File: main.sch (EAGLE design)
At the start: 116 parts, among them IC10 FGPMMOPA6H, IC2 25LC1024-I/P, IC6 MPL3115A2LGA, IC7 FXAS21000, IC8 ADXL343BCCZ, Q1 12MHz, Q2 MCP9700A-E/TO, Q3 FQP7P06, Q4 MCP9700A-E/TO, U1 ATMEGA1284P-PU, U2 LT3570EFEPBF, U3 TL431BQLP, X1 132134RP

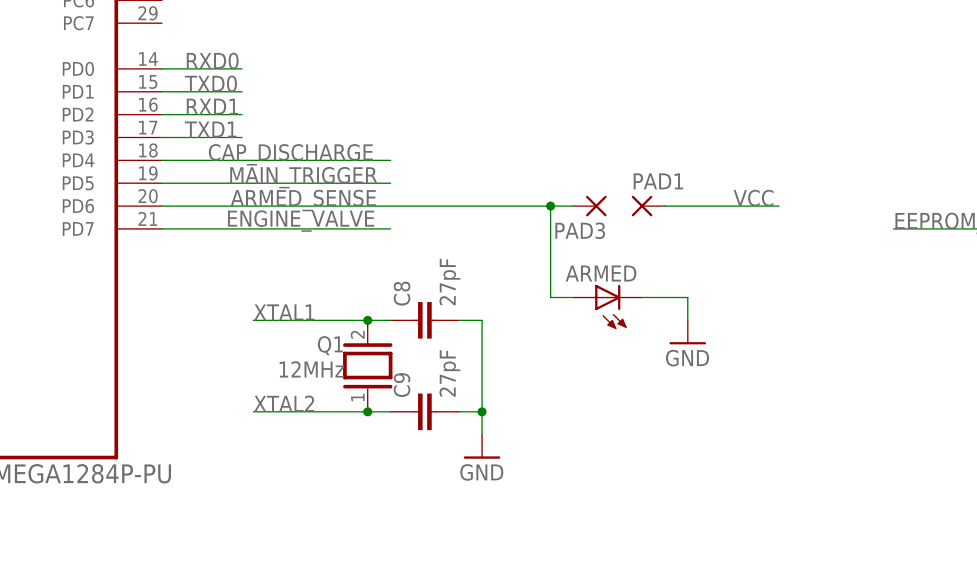
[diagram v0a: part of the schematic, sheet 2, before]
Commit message: Changed armed sense so that the pin is pulled low when armed and added resistor for armed LED.
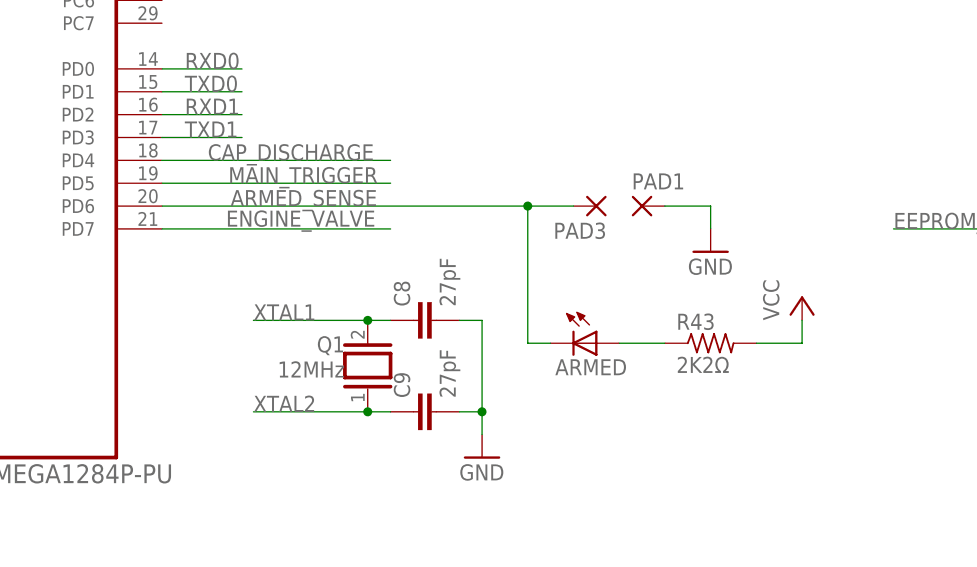
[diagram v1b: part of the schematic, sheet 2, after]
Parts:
- added R43: 2K2Ω, rcl:R-US_0207/5V
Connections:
- new net N$33: ARMED.A, R43.1
- net ARMED_SENSE: now also ARMED.C; no longer ARMED.A
- net GND: now also PAD1.P; no longer ARMED.C
- net VCC: now also R43.2; no longer PAD1.P
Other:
- moved on the sheet: ARMED
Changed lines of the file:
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@@
 <?xml version="1.0" encoding="utf-8"?>
 <!DOCTYPE eagle SYSTEM "eagle.dtd">
-<eagle version="8.6.0">
+<eagle version="8.5.1">
 <drawing>
 <settings>
@@
 <part name="ARMED" library="led" library_urn="urn:adsk.eagle:library:259" deviceset="LED" device="5MM" package3d_urn="urn:adsk.eagle:package:15799/2"/>
 <part name="GND35" library="supply1" library_urn="urn:adsk.eagle:library:371" deviceset="GND" device=""/>
+<part name="R43" library="rcl" library_urn="urn:adsk.eagle:library:334" deviceset="R-US_" device="0207/5V" package3d_urn="urn:adsk.eagle:package:23502/1" value="2K2Ω"/>
+<part name="P+8" library="supply1" library_urn="urn:adsk.eagle:library:371" deviceset="VCC" device=""/>
 </parts>
 <sheets>
@@
 <instance part="PAD1" gate="1" x="134.62" y="114.3"/>
 <instance part="PAD3" gate="1" x="129.54" y="114.3" rot="R180"/>
-<instance part="ARMED" gate="G$1" x="129.54" y="104.14" rot="R90"/>
-<instance part="GND35" gate="1" x="139.7" y="99.06"/>
+<instance part="ARMED" gate="G$1" x="129.54" y="99.06" rot="R270"/>
+<instance part="GND35" gate="1" x="142.24" y="109.22"/>
+<instance part="R43" gate="G$1" x="142.24" y="99.06"/>
+<instance part="P+8" gate="VCC" x="152.4" y="104.14"/>
 </instances>
 <busses>
@@
 </segment>
 <segment>
-<pinref part="ARMED" gate="G$1" pin="C"/>
-<wire x1="134.62" y1="104.14" x2="139.7" y2="104.14" width="0.1524" layer="91"/>
-<wire x1="139.7" y1="104.14" x2="139.7" y2="101.6" width="0.1524" layer="91"/>
+<pinref part="PAD1" gate="1" pin="P"/>
 <pinref part="GND35" gate="1" pin="GND"/>
+<wire x1="137.16" y1="114.3" x2="142.24" y2="114.3" width="0.1524" layer="91"/>
+<wire x1="142.24" y1="114.3" x2="142.24" y2="111.76" width="0.1524" layer="91"/>
 </segment>
 </net>
@@
 </segment>
 <segment>
-<wire x1="137.16" y1="114.3" x2="149.86" y2="114.3" width="0.1524" layer="91"/>
-<label x="144.78" y="114.3" size="1.778" layer="95"/>
-<pinref part="PAD1" gate="1" pin="P"/>
+<pinref part="P+8" gate="VCC" pin="VCC"/>
+<wire x1="152.4" y1="101.6" x2="152.4" y2="99.06" width="0.1524" layer="91"/>
+<pinref part="R43" gate="G$1" pin="2"/>
+<wire x1="152.4" y1="99.06" x2="147.32" y2="99.06" width="0.1524" layer="91"/>
 </segment>
 </net>
@@
 <label x="88.9" y="114.3" size="1.778" layer="95"/>
 <pinref part="U1" gate="A" pin="PD6"/>
-<wire x1="81.28" y1="114.3" x2="124.46" y2="114.3" width="0.1524" layer="91"/>
+<wire x1="81.28" y1="114.3" x2="121.92" y2="114.3" width="0.1524" layer="91"/>
 <pinref part="PAD3" gate="1" pin="P"/>
-<pinref part="ARMED" gate="G$1" pin="A"/>
-<wire x1="124.46" y1="114.3" x2="127" y2="114.3" width="0.1524" layer="91"/>
-<wire x1="124.46" y1="114.3" x2="124.46" y2="104.14" width="0.1524" layer="91"/>
-<wire x1="124.46" y1="104.14" x2="127" y2="104.14" width="0.1524" layer="91"/>
-<junction x="124.46" y="114.3"/>
+<pinref part="ARMED" gate="G$1" pin="C"/>
+<wire x1="121.92" y1="114.3" x2="127" y2="114.3" width="0.1524" layer="91"/>
+<wire x1="124.46" y1="99.06" x2="121.92" y2="99.06" width="0.1524" layer="91"/>
+<wire x1="121.92" y1="99.06" x2="121.92" y2="114.3" width="0.1524" layer="91"/>
+<junction x="121.92" y="114.3"/>
 </segment>
 </net>
@@
 </segment>
 </net>
+<net name="N$33" class="0">
+<segment>
+<pinref part="R43" gate="G$1" pin="1"/>
+<pinref part="ARMED" gate="G$1" pin="A"/>
+<wire x1="137.16" y1="99.06" x2="132.08" y2="99.06" width="0.1524" layer="91"/>
+</segment>
+</net>

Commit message: Fixed ERC errors and renumbered all components.
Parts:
- removed C33, C34: 0.1µF, rcl:C-EU025-025X050
- removed IC8: ADXL343BCCZ, CU in Space:ADXL343BCCZ
- removed U$10, U$9: TEST, Power:TEST
- added C25: 22µF, Power:UST1V220MDD
- added C29: 10nF, Power:K103K15X7RF5TL2
- added IC5: 25LC1024-I/P, microchip:25LC080P
- added U$7: CAP, Power:TEST
- added U$8: BAT+, Power:TEST
- ARMED: value (none) -> RED
- C10: value 47pF -> 0.1µF
- C11: value 1µF -> 0.1µF
- C12: value 1nF -> 0.1µF; device Power:K102K15X7RF5TL2 -> rcl:C-EU025-025X050
- C13, C14: value 22µF -> 0.1µF; device Power:UST1V220MDD -> rcl:C-EU025-025X050
- C15: value 1nF -> 2.2µF; device Power:K102K15X7RF5TL2 -> rcl:C-EU025-025X050
- C16: value 10nF -> 27pF; device Power:K103K15X7RF5TL2 -> rcl:C-EU025-025X050
- C17: value 0.1µF -> 27pF
- C19: value 22µF -> 47pF; device Power:UST1V220MDD -> rcl:C-EU025-025X050
- C20: value 0.1µF -> 1µF
- C26, C27: value 0.1µF -> 22µF; device rcl:C-EU025-025X050 -> Power:UST1V220MDD
- C30: value 10µF -> 1nF; device rcl:CPOL-USE2-5 -> Power:K102K15X7RF5TL2
- C31: value 10µF -> 10nF; device rcl:CPOL-USE2-5 -> Power:K103K15X7RF5TL2
- C32: value 0.1µF -> 1nF; device rcl:C-EU025-025X050 -> Power:K102K15X7RF5TL2
- C4: value 2.2µF -> 0.1µF
- C6: value 0.1µF -> 10µF; device rcl:C-EU025-025X050 -> rcl:CPOL-USE2-5
- C7: value 10nF -> 0.1µF; device Power:K103K15X7RF5TL2 -> rcl:C-EU025-025X050
- C8: value 27pF -> 10µF; device rcl:C-EU025-025X050 -> rcl:CPOL-USE2-5
- C9: value 27pF -> 0.1µF
- IC2: value 25LC1024-I/P -> ADXL343BCCZ; device microchip:25LC080P -> CU in Space:ADXL343BCCZ
- L1: value 18µH -> 10µH; device Power:RLB0914-180KL -> rcl:L-US0207/5V
- L2: value 10µH -> 18µH; device rcl:L-US0207/5V -> Power:RLB0914-180KL
- Q1: value 12MHz -> MCP9700A-E/TO; device special:XTAL/S -> CU in Space:MCP9700A-E/TO
- Q3: value FQP7P06 -> 12MHz; device Power:FQP7P06 -> special:XTAL/S
- Q4: value MCP9700A-E/TO -> FQP7P06; device CU in Space:MCP9700A-E/TO -> Power:FQP7P06
- R10: value 24.9kΩ -> 2K2Ω; device Power:MFR-25FBF52-24K9 -> rcl:R-US_0207/5V
- R11: value 24.9kΩ -> 1MΩ; device Power:MFR-25FBF52-24K9 -> rcl:R-US_0207/5V
- R12: value 51.1kΩ -> 1M; device Power:MFR-25FBF52-51K1 -> Power:MFR-25FBF52-3K65
- R13: value 17.4kΩ -> 3.6k; device Power:MFR-25FBF52-17K4 -> Power:MFR-25FBF52-3K65
- R14: value 3.65kΩ -> 1MΩ; device Power:MFR-25FBF52-3K65 -> rcl:R-US_0207/5V
- R15, R16: value 51.1kΩ -> 750; device Power:MFR-25FBF52-51K1 -> Power:MFR-25FBF52-3K65
- R17, R18: value 47kΩ -> 750; device rcl:R-US_0207/5V -> Power:MFR-25FBF52-3K65
- R19: value 2K2Ω -> 750; device rcl:R-US_0207/5V -> Power:MFR-25FBF52-3K65
- R2: value 1MΩ -> (none); device rcl:R-US_0207/5V -> Power:MFR-25FBF52-3K65
- R3: value 1MΩ -> 4k7Ω
- R30: value 750 -> ~1.4k
- R31, R34: value 750 -> 51.1kΩ; device Power:MFR-25FBF52-3K65 -> Power:MFR-25FBF52-51K1
- R32: value 750 -> 24.9kΩ; device Power:MFR-25FBF52-3K65 -> Power:MFR-25FBF52-24K9
- R33: value 750 -> 3.65kΩ
- R35: value (none) -> 17.4kΩ; device Power:MFR-25FBF52-3K65 -> Power:MFR-25FBF52-17K4
- R36: value (none) -> 8.06kΩ; device Power:MFR-25FBF52-3K65 -> Power:MFR-25FBF52-8K06
- R37: value 1M -> 3.65kΩ
- R38: value 1M -> 24.9kΩ; device Power:MFR-25FBF52-3K65 -> Power:MFR-25FBF52-24K9
- R39: value 3.6k -> 1M
- R4: value 10kΩ -> 4k7Ω
- R40: value 3.6k -> 51.1kΩ; device Power:MFR-25FBF52-3K65 -> Power:MFR-25FBF52-51K1
- R42: value ~1.4k -> 51.1kΩ; device Power:MFR-25FBF52-3K65 -> Power:MFR-25FBF52-51K1
- R43: value 2K2Ω -> 3.6k; device rcl:R-US_0207/5V -> Power:MFR-25FBF52-3K65
- R5, R6: value 4k7Ω -> 47kΩ
- R7: value 8.06kΩ -> (none); device Power:MFR-25FBF52-8K06 -> Power:MFR-25FBF52-3K65
- R8: value 51.1kΩ -> 10kΩ; device Power:MFR-25FBF52-51K1 -> rcl:R-US_0207/5V
- R9: value 3.65kΩ -> 2K2Ω; device Power:MFR-25FBF52-3K65 -> rcl:R-US_0207/5V
- U$1: value +3.3V -> TEST
- U$2: value +24V -> TEST
- U$3: value BAT+ -> CAP
- U$4: value CAP -> BAT+
- U$5: value CAP -> +24V
- U$6: value BAT+ -> +3.3V
- renumbered IC10 to IC4, IC6 to IC3, IC7 to IC1, PAD6 to PAD4, XB2 to XB1
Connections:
- removed net ENGINE_VALVE: U1.PD7
- removed net N$75: R42.22, T3.C
- new net N$34: R30.11, T1.C
- net +12.0: now also C25.+, D3.C, R15.11, R16.11, R17.11, R18.11, R19.11, R42.11; no longer C14.+, D1.C, R30.11, R31.11, R32.11, R33.11, R34.11, R8.11
- net 12V_ENABLE: now also U$2.P$1; no longer U$10.P$1
- net ACCEL_INT: now also IC2.INT1; no longer IC8.INT1
- net AREF: now also C14.1; no longer C6.1
- net ARMED_SENSE: now also PAD2.P; no longer PAD3.P
- net AVCC: now also C11.2, C9.2, L1.2, Q1.VDD; no longer C18.2, C5.2, L2.2, Q4.VDD
- net A_GND: now also C11.1, C12.2, C14.2, C9.1, Q1.GND, R2.22, R6.1; no longer C18.1, C21.2, C5.1, C6.2, Q4.GND, R18.1, R36.22
- net BAT+: now also Q4.S, R33.11, R34.11, R5.2, U$8.P$1; no longer Q3.S, R14.11, R15.11, R17.2, U$6.P$1
- net BAT_REF: now also C12.1, R5.1, R6.2; no longer C21.1, R17.1, R18.2
- net CAP_DISCHARGE: now also R13.11; no longer R41.11
- net CAP_REF: now also R2.11, R7.22, U$1.P$1; no longer R35.22, R36.11, U$9.P$1
- net EEPROM_CS: now also IC5.!CS, R14.1; no longer IC2.!CS, R2.1
- net FB1: now also R37.11, R42.22; no longer R8.22, R9.11
- net GND: now also C13.2, C18.1, C19.2, C20.2, C21.2, C25.-, C26.-, C27.-, C29.2, C30.2, C31.2, C5.2, C6.-, C8.-, IC2.GND_2, IC2.GND_3, IC2.SDO/ALT_ADDRESS, IC5.!HOLD, IC5.!WP, IC5.GND, R10.2, R12.11, R31.22, R35.11, R36.11, R37.22, R39.11, U$3.P$1; no longer C11.2, C12.2, C13.-, C14.-, C19.-, C26.2, C27.2, C28.2, C30.-, C31.-, C33.2, C34.1, C8.2, C9.2, IC2.!HOLD, IC2.!WP, IC8.GND, IC8.GND_2, IC8.GND_3, IC8.SDO/ALT_ADDRESS, R13.11, R16.22, R19.2, R37.11, R38.11, R7.11, R9.22, U$5.P$1
- net MAIN_TRIGGER: now also R39.22, R41.11, R43.11; no longer R38.22, R39.11, R40.11
- net MISO: now also IC5.SO; no longer IC2.SO
- net MOSI: now also IC5.SI; no longer IC2.SI
- net N$1: now also C5.1; no longer C1.1
- net N$10: now also C32.1, R38.11; no longer C12.1, R10.11
- net N$11: now also R32.11; no longer R11.11
- net N$12: now also C29.1; no longer C16.1
- net N$13: now also C28.2; no longer C20.2
- net N$15: now also R35.22, R40.11; no longer R12.11, R13.22
- net N$16: now also C28.1, D1.C; no longer C20.1, D3.C
- net N$3: now also C13.1; no longer C27.1
- net N$33: now also R9.1; no longer R43.1
- net N$5: now also C31.1; no longer C7.1
- net N$6: now also R36.22; no longer R7.22
- net N$69: now also Q4.G, R33.22; no longer Q3.G, R14.22
- net N$7: now also R38.22; no longer R10.22
- net N$70: now also R31.11, R34.22; no longer R15.22, R16.11
- net N$71: now also R10.1; no longer R19.1
- net N$77: now also T3.C; no longer T1.C
- net N$79: now also R43.22, T3.B; no longer R39.22, T1.B
- net N$8: now also D3.A, L2.2, U$5.P$1; no longer D1.A, L1.2, U$2.P$1
- net N$80: now also R41.22; no longer R40.22
- net N$81: now also PAD3.P, R15.22, R16.22, R17.22, R18.22, R19.22, R7.11, U$7.P$1; no longer PAD2.P, R31.22, R32.22, R33.22, R34.22, R35.11, R42.11, U$4.P$1
- net N$82: now also R12.22, R13.22, T1.B; no longer R37.22, R41.22, T3.B
- net N$9: now also C30.1, R32.22; no longer C15.1, R11.22
- net PWR_JUNC: now also C27.+, L2.1, Q4.D, U$4.P$1; no longer C13.+, L1.1, Q3.D, U$3.P$1
- net RADIO_CS: now also R11.1; no longer R3.1
- net RESET: now also R8.1; no longer R4.1
- net SCK: now also IC5.SCK; no longer IC2.SCK
- net SCL: now also IC2.SCL/SCLK, R3.1; no longer IC8.SCL/SCLK, R5.1
- net SDA: now also IC2.SDA/SDI/SDIO, R4.1; no longer IC8.SDA/SDI/SDIO, R6.1
- net TEMP: now also Q1.VOUT; no longer Q2.VOUT
- net TEMP2: now also Q2.VOUT; no longer Q4.VOUT
- net VCC: now also C1.1, C15.1, C18.2, C19.1, C20.1, C21.1, C26.+, C6.+, C7.1, C8.+, D1.A, IC2.!CS, IC2.VDD_I/O, IC2.VS, IC5.VCC, L1.1, R11.2, R14.2, R40.22, R8.2, R9.2, U$6.P$1; no longer C11.1, C17.1, C19.+, C26.1, C28.1, C30.+, C31.+, C32.1, C33.1, C34.2, D3.A, IC2.VCC, IC8.!CS, IC8.VDD_I/O, IC8.VS, L2.1, R12.22, R2.2, R43.2, R5.2, R6.2, U$1.P$1
- net XTAL1: now also C17.1, Q3.2; no longer C8.1, Q1.2
- net XTAL2: now also C16.1, Q3.1; no longer C9.1, Q1.1

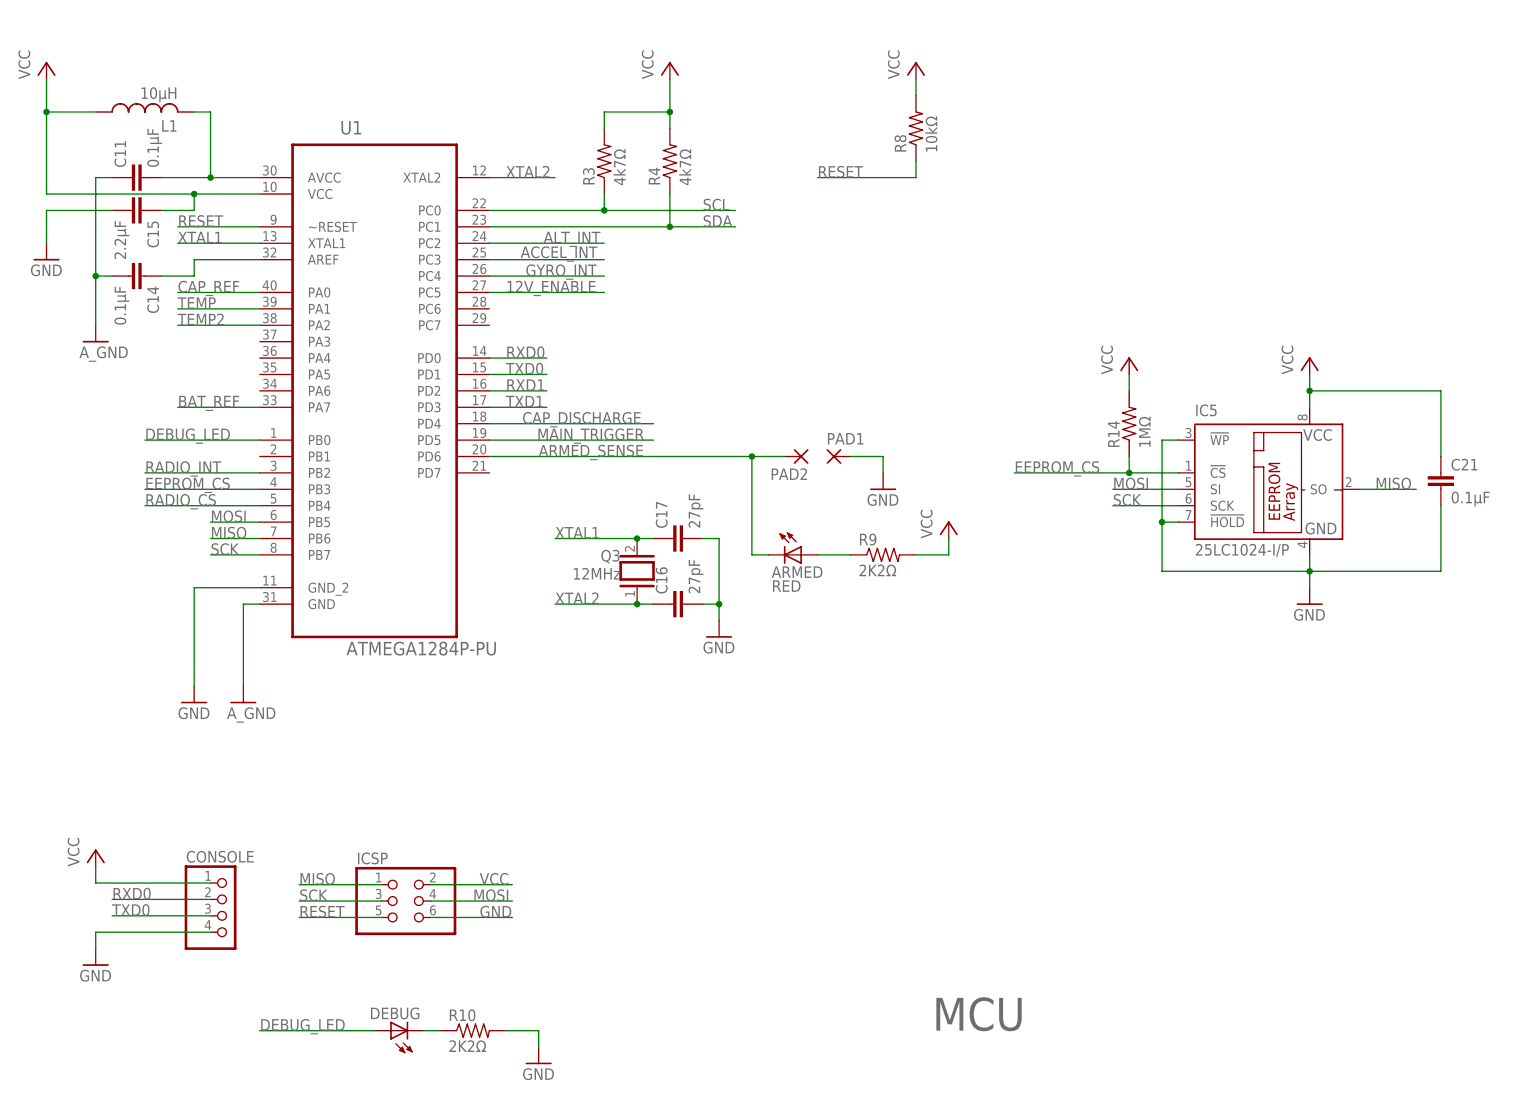
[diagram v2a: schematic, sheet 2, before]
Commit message: Relayed-out digital section.
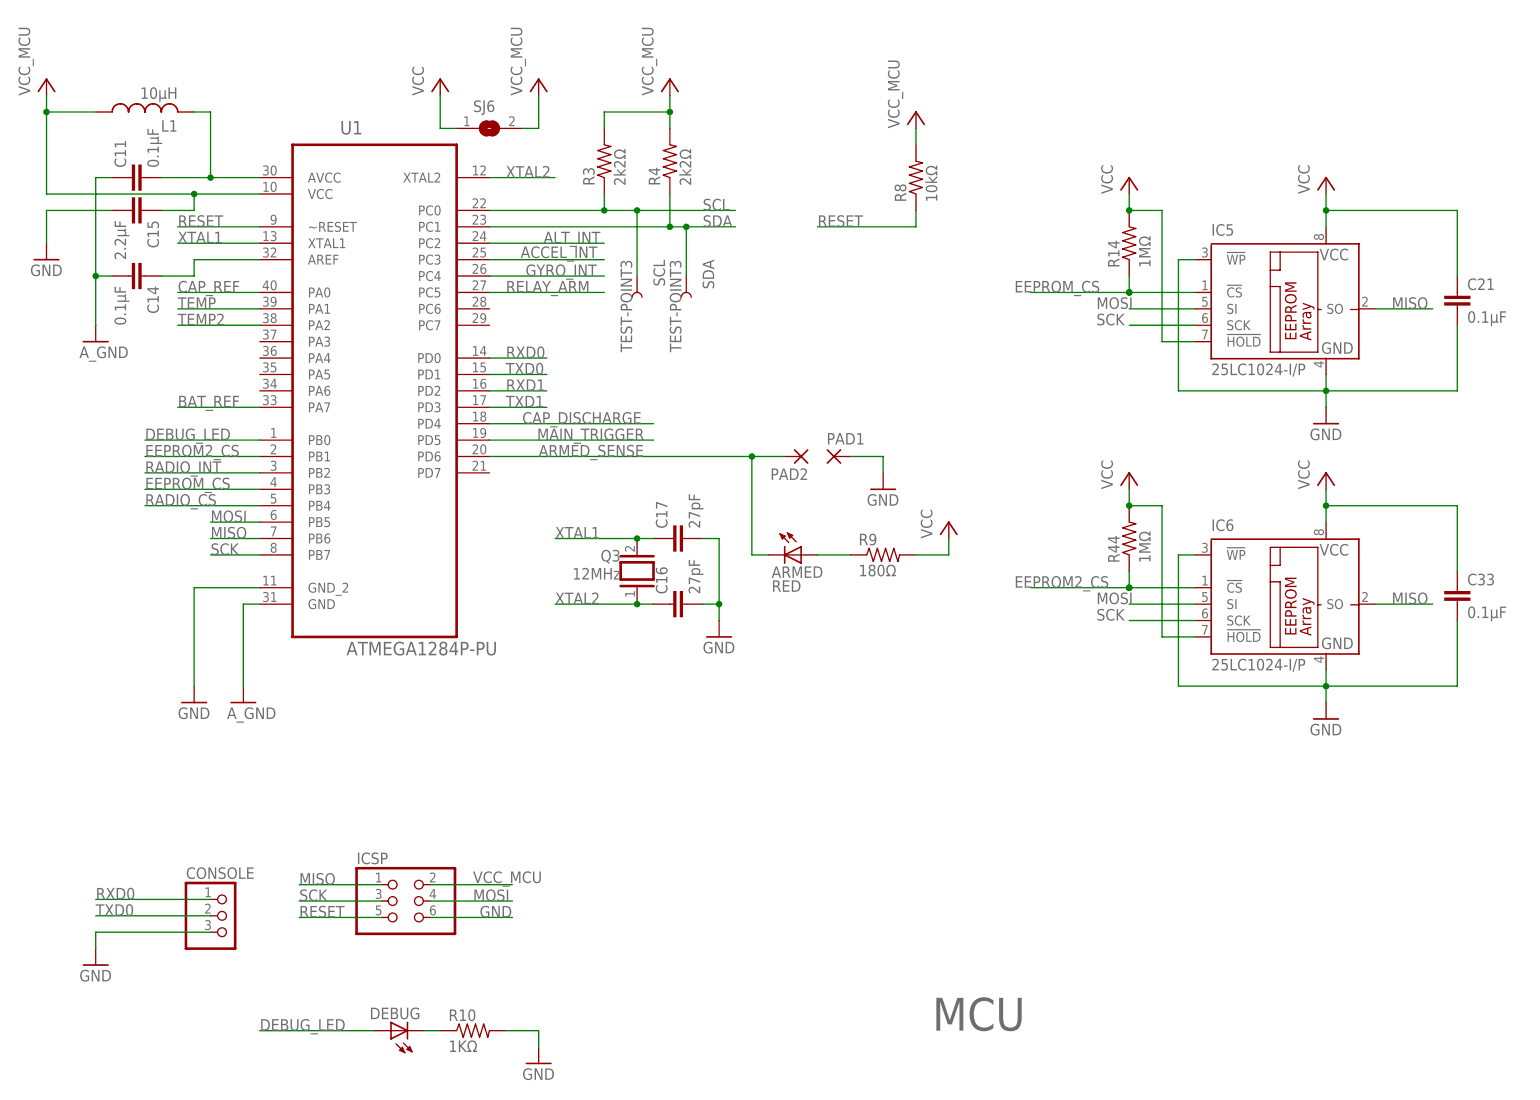
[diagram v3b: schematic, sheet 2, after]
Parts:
- added C33: 0.1µF, rcl:C-EU025-025X050
- added IC6: 25LC1024-I/P, microchip:25LC080P
- added R44: 1MΩ, rcl:R-US_0207/5V
- added SCL, SDA: TEST-POINT3, SparkFun-Connectors:TEST-POINT3
- added SJ1, SJ2, SJ3, SJ4, SJ5, SJ6: (no value), jumper:SJ
- CONSOLE: device pinhead:PINHD-1X4 -> pinhead:PINHD-1X3
- R10: value 2K2Ω -> 1KΩ
- R3, R4: value 4k7Ω -> 2k2Ω
- R9: value 2K2Ω -> 180Ω
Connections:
- new net EEPROM2_CS: IC6.!CS, R44.1, U1.PB1
- new net RELAY_ARM: U1.PC5
- new net VCC_ACCEL: C4.1, C6.+, C7.1, IC2.!CS, IC2.VDD_I/O, IC2.VS, SJ3.2
- new net VCC_ALT: C10.1, C8.+, IC3.VDD, IC3.VDDIO, SJ2.2
- new net VCC_GPS: C18.2, IC4.VCC, SJ5.2
- new net VCC_GYRO: C1.1, C2.1, C3.1, IC1.I2C/!SPI, IC1.VDDIO, IC1.VDD_33, R1.1, SJ1.2
- new net VCC_MCU: C15.1, ICSP.2, L1.1, R11.2, R3.2, R4.2, R8.2, SJ6.2, U1.VCC
- new net VCC_XB: C19.1, C20.1, SJ4.2, XB1.VCC
- net 12V_ENABLE: no longer U1.PC5
- net GND: now also C33.2, CONSOLE.3, IC6.!WP, IC6.GND; no longer CONSOLE.4, IC5.!HOLD
- net MISO: now also IC6.SO
- net MOSI: now also IC6.SI
- net RXD0: now also CONSOLE.1; no longer CONSOLE.2
- net SCK: now also IC6.SCK
- net SCL: now also SCL.1
- net SDA: now also SDA.1
- net TXD0: now also CONSOLE.2; no longer CONSOLE.3
- net VCC: now also C33.1, IC5.!HOLD, IC6.!HOLD, IC6.VCC, R44.2, SJ1.1, SJ2.1, SJ3.1, SJ4.1, SJ5.1, SJ6.1; no longer C1.1, C10.1, C15.1, C18.2, C19.1, C2.1, C20.1, C3.1, C4.1, C6.+, C7.1, C8.+, CONSOLE.1, IC1.I2C/!SPI, IC1.VDDIO, IC1.VDD_33, IC2.!CS, IC2.VDD_I/O, IC2.VS, IC3.VDD, IC3.VDDIO, IC4.VCC, ICSP.2, L1.1, R1.1, R11.2, R3.2, R4.2, R8.2, U1.VCC, XB1.VCC
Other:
- moved on the sheet: C21, C9, IC5, Q1, Q2, R14, R8
